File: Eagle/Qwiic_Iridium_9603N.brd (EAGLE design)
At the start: 50.8 x 50.8 mm, 72 parts, among them J1 SS4-10-3.50-X-D, J3 PTH, J6 ISP, J7 U.FL, Q1 DMG3415U-7, Q2 2N2222, U1 ATTINY84-ARDUINO, U2 LTC3225EDDB#TRMPBF

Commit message: Updates for V2 of the PCB
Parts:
- removed S1, S2: STANDOFF_ELECTRICALMCMASTER-95117A411, SparkFun-Electromechanical:STANDOFF-ELECTRICAL-MCMASTER-95117A411
- removed U$47: (no value), Labels:QWIIC-LOGO-MEDIUM
- added J8: (no value), SparkFun-Connectors:1X01_NO_SILK
- added U$10: (no value), 9603N_POWER:9603N_POWER0
- added U$11, U$28: (no value), 5.3V_OUT:5#3V0
- added U$12, U$17: (no value), Qwiic_007:QWIIC0
- added U$13: (no value), 150mA:150MA0
- added U$14: (no value), Charge:CHARGE0
- added U$15: (no value), Current:CURRENT0
- added U$18, U$19: (no value), Iridium_007:IRIDIUM0
- added U$2: (no value), POWER:POWER0
- added U$20, U$24: (no value), 9603N_007:9603N0
- added U$25: (no value), Qwiic_Bubble:QWIIC0
- added U$9: (no value), CHARGING:CHARGING0
- ANTENNA: device con-coax:J502-ND-142-0711-821/826 -> Qwiic_Iridium_9603N:J502-ND-142-0711-821/826
- J1: value SS4-10-3.50-X-D -> IRIDIUM_9603NIRIDIUM_9603N; device SS4-10-3.50-X-D:SS4-10-3.50-X-D -> Qwiic_Iridium_9603N:IRIDIUM_9603N
- U$1: device Labels:QWIIC-LOGO-MEDIUM -> 60mA:60MA0
- U$23: device buzzard_labels (3):QWIIC0 -> Qwiic_Bubble:QWIIC0
- U2: device LTC_By_element14_Batch_1:DFN300X200-10L -> Qwiic_Iridium_9603N:DFN300X200-10L
- moved J1 27.6 mm to (12.7, 8.89)
- moved U$1 11.8 mm to (44.7, 37.0), flipped to the top, turned to 90 degrees
- moved U$23 8.71 mm to (8.51, 21.2), turned to 90 degrees
- moved FRAME1 3.81 mm to (-7.62, -14.0)
- moved LOGO1 2.54 mm to (38.1, 2.54)
- moved J3 1.27 mm to (19.1, 1.27)
- moved J5 1.27 mm to (29.2, 1.27)
- moved U$16 1.27 mm to (29.2, 1.52)
- moved U$21 1.27 mm to (21.6, 1.65)
- moved U$22 1.27 mm to (19.1, 1.65)
- moved U$26 1.27 mm to (26.7, 1.65)
- moved U$27 1.27 mm to (24.1, 1.65)
- moved U$3 1.27 mm to (19.1, 1.65)
- moved U$4 1.27 mm to (21.6, 1.65)
- moved U$5 1.27 mm to (24.1, 1.65)
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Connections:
- net EXT_PWR: now also J8.1
- net GND: now also J1.HOLE1, J1.HOLE2; no longer S1.P1, S2.P1
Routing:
- net EXT_PWR: track 37.3 -> 58.4 mm
- net GND: track 35.8 -> 37.3 mm
- net 3.3V: track 131.4 -> 130.5 mm
- net SDA: track 93.1 -> 93.6 mm
- net !RST: track 51.7 -> 51.2 mm
- net SCL: track 88.2 -> 88.7 mm
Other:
- board text added: "V2"
- board text removed: "9603_Power"
- board text removed: "Charge Current 60mA 150mA"
- board text removed: "Charging"
- board text removed: "Power"
- board text removed: "Qwiic RockBLOCK 9603N"
- board text removed: "TPA2005D1"
- board text removed: "V1"

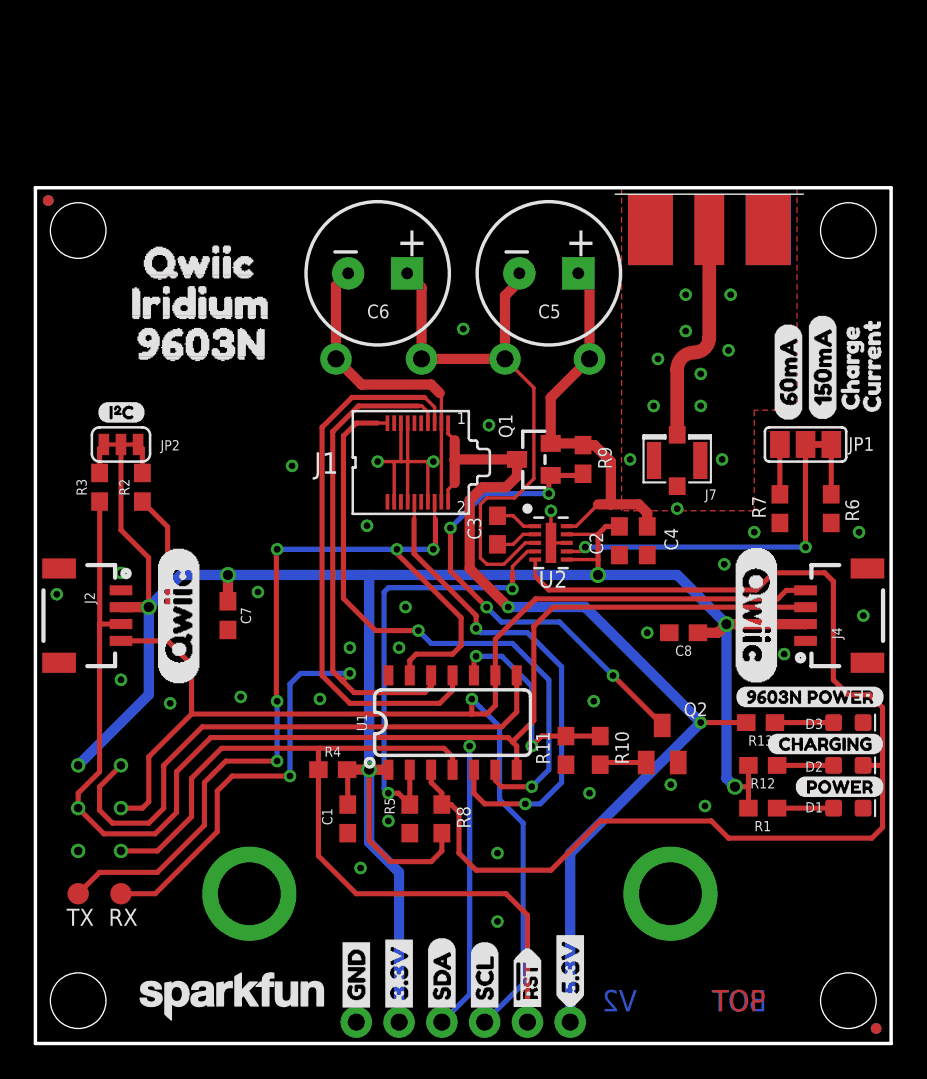
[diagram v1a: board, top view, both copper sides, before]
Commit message: Substantial update after testing the PCB
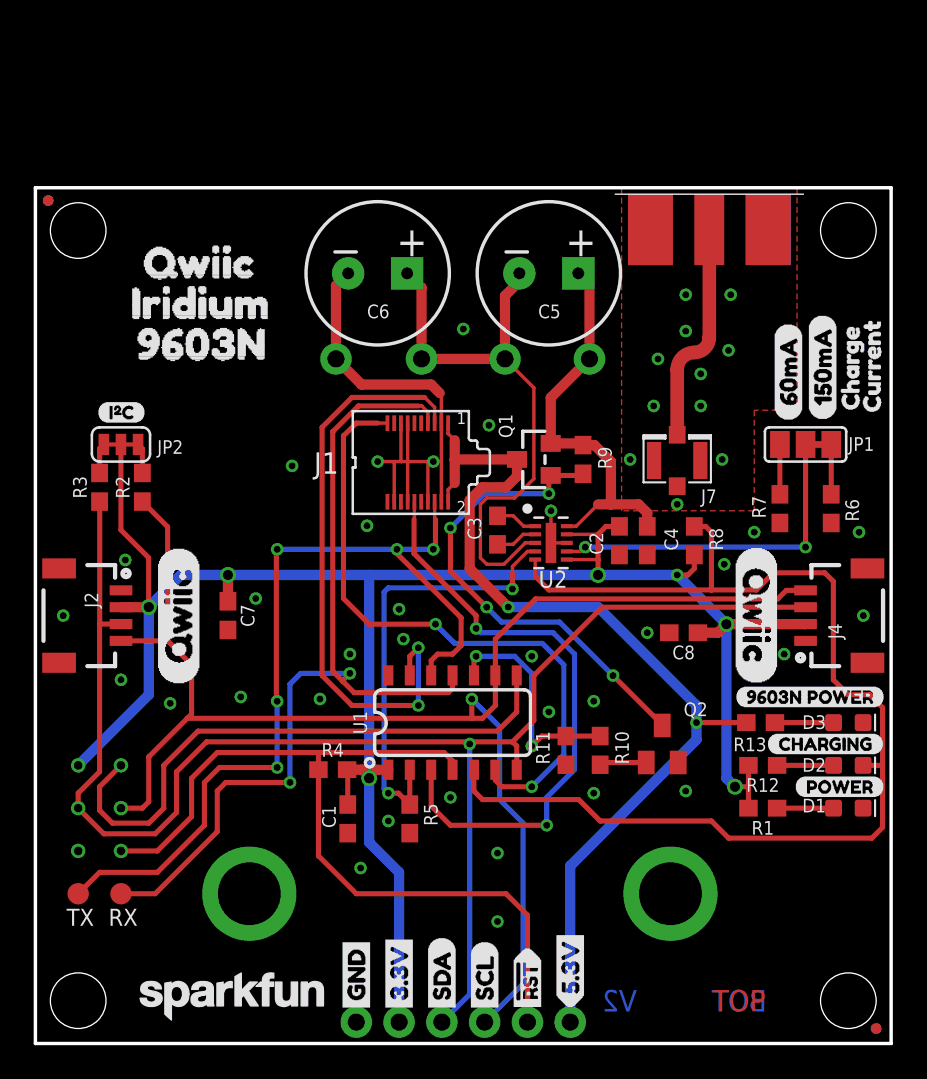
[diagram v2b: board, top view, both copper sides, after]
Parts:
- ANTENNA: value SMA-142-0711-821/826 -> SMA-; device Qwiic_Iridium_9603N:J502-ND-142-0711-821/826 -> Qwiic_Iridium_9603N:J502-ND-142-0711-821/826_NO_CREAM
- JP1: value (none) -> JUMPER-PAD-3-2OF3_NC_BY_TRACE_LARGE; device SparkFun-Passives:PAD-JUMPER-3-2OF3_NC_BY_TRACE_YES_SILK_LARGE -> Qwiic_Iridium_9603N:PAD-JUMPER-3-2OF3_NC_BY_TRACE_YES_SILK_LARGE
- U1: value ATTINY84-ARDUINO -> ATTINY841-ARDUINO; device SparkFun-IC-Microcontroller:SO14 -> Qwiic_Iridium_9603N:SO14
- moved R8 22.3 mm to (39.1, 29.8)
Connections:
- net ON_OFF: now also U1.13; no longer U1.11
- net PGOOD: now also U1.5; no longer U1.3
- net RI: now also U1.3; no longer U1.5
- net RX(OUT): now also U1.11; no longer U1.12
- net TX(IN): now also U1.12; no longer U1.13
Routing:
- net 3.3V: track 130.5 -> 122.7 mm, vias 6 -> 7
- net RI: track 29.3 -> 35.9 mm
- net SDA: track 93.6 -> 91.4 mm
- net ON_OFF: track 33.0 -> 35.1 mm, vias 0 -> 2
- net PGOOD: track 70.8 -> 68.9 mm
- net NA: track 36.5 -> 38.3 mm
- net RX(OUT): track 52.7 -> 54.3 mm
- net TX(IN): track 52.9 -> 51.9 mm
- net !RST: track 51.2 -> 50.5 mm
- net SCL: track 88.7 -> 89.3 mm
- net GND: vias 42 -> 44

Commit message: Added the ADM4210
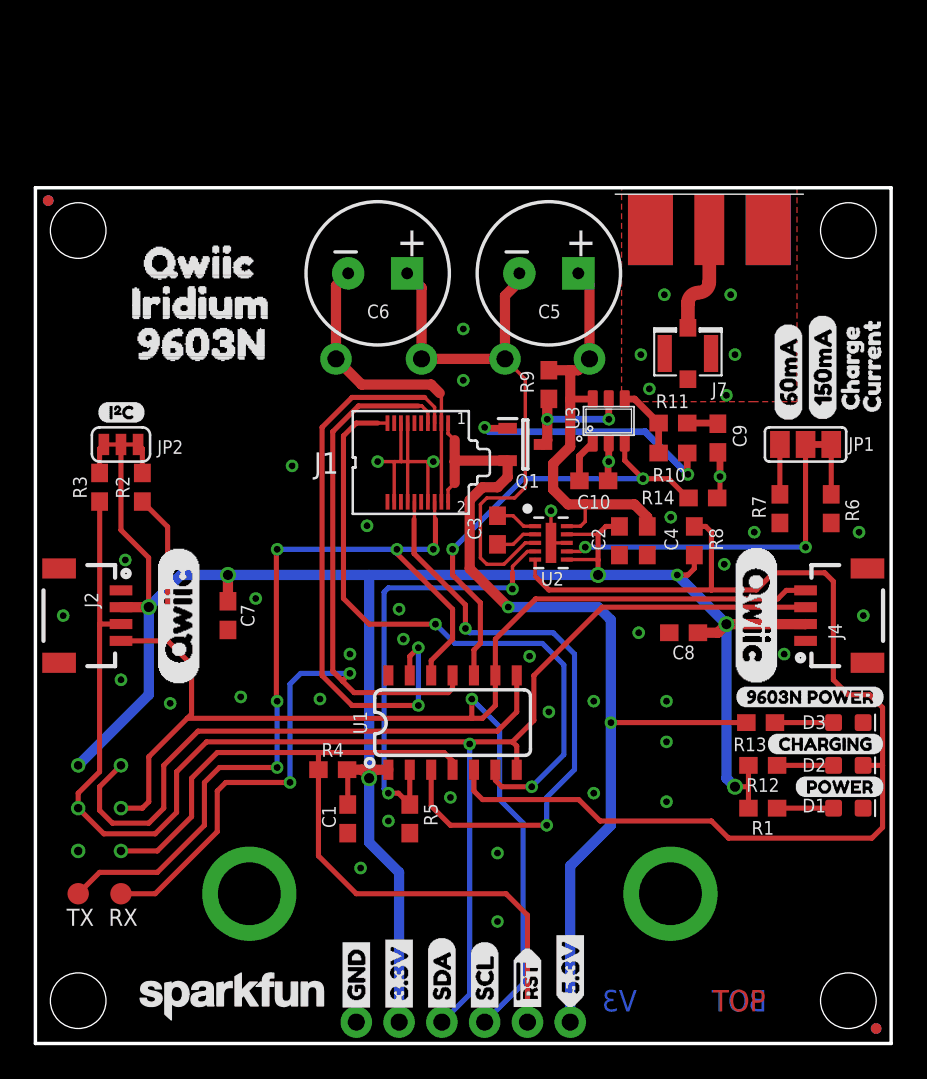
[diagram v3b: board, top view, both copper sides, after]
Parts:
- removed Q2: 2N2222, transistor:SOT23-BEC
- added C10: 0.22uF, SparkFun-Capacitors:0603
- added C9: 10nF, SparkFun-Capacitors:0603
- added R14: 10k, SparkFun-Resistors:0603
- added U3: ADM4210-1, ADM4210:TSOT6
- J1: value IRIDIUM_9603NIRIDIUM_9603N -> IRIDIUM_9603N
- Q1: value DMG3415U-7 -> DMG3414U-7; device microbuilder:SOT23-WIDE -> DMG3414U-7:SOT96P240X100-3N
- R10: value 1k -> 100
- R11: value 10k -> 100
- R9: value 10k -> 0.012 Ohm
- moved R11 20.4 mm to (37.8, 36.8), turned to 0 degrees
- moved R10 18.2 mm to (37.8, 35.1), turned to 180 degrees
- moved J7 6.38 mm to (38.7, 41.0)
- moved R9 4.89 mm to (30.5, 39.1), turned to 90 degrees
- moved Q1 1.02 mm to (29.1, 35.6), turned to 0 degrees
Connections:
- removed net N$19: Q1.1, Q2.C, R9.2
- removed net N$20: Q2.B, R10.2
- new net N$12: Q1.1, R10.1
- new net N$13: R10.2, R11.1, U3.4
- new net N$14: C9.1, R11.2
- new net N$15: C10.1, U3.1
- new net N$8: Q1.3, R9.1, U3.5
- net EXT_PWR: now also Q1.2; no longer Q1.3
- net GND: now also C10.2, C9.2, R14.2, U3.2; no longer Q2.E, R11.2
- net LTC3225_VOUT: now also R9.2, U3.6; no longer Q1.2, R9.1
- net PWR_EN: now also R14.1, U3.3; no longer R10.1, R11.1
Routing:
- net N$19: track 28.7 -> 0.00 mm, vias 4 -> 0
- net N$12: track 0.00 -> 15.9 mm, vias 0 -> 2
- net PWR_EN: track 13.5 -> 27.1 mm
- net N$8: track 0.00 -> 7.71 mm, vias 0 -> 2
- net N$7: track 13.0 -> 6.34 mm
- net GND: track 37.3 -> 42.4 mm
- net N$13: track 0.00 -> 4.38 mm
- net N$20: track 2.79 -> 0.00 mm
- net N$15: track 0.00 -> 2.58 mm
- net N$14: track 0.00 -> 1.83 mm
- net LTC3225_VOUT: track 24.2 -> 25.9 mm
- net TX(IN): track 51.9 -> 50.9 mm
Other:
- board text added: "V3"
- board text removed: "V2"

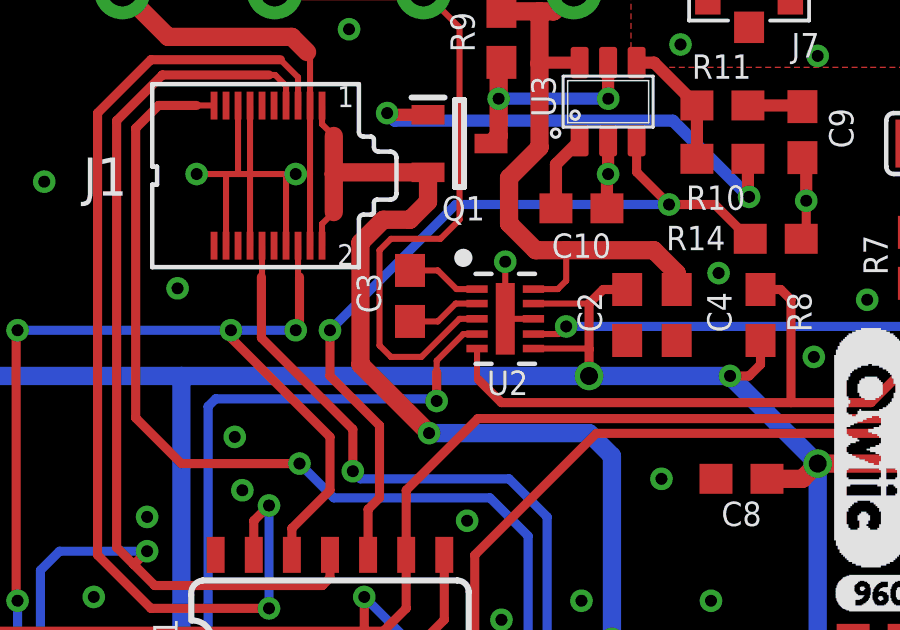
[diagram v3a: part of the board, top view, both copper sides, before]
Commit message: Added assembly details for V3 of the PCB
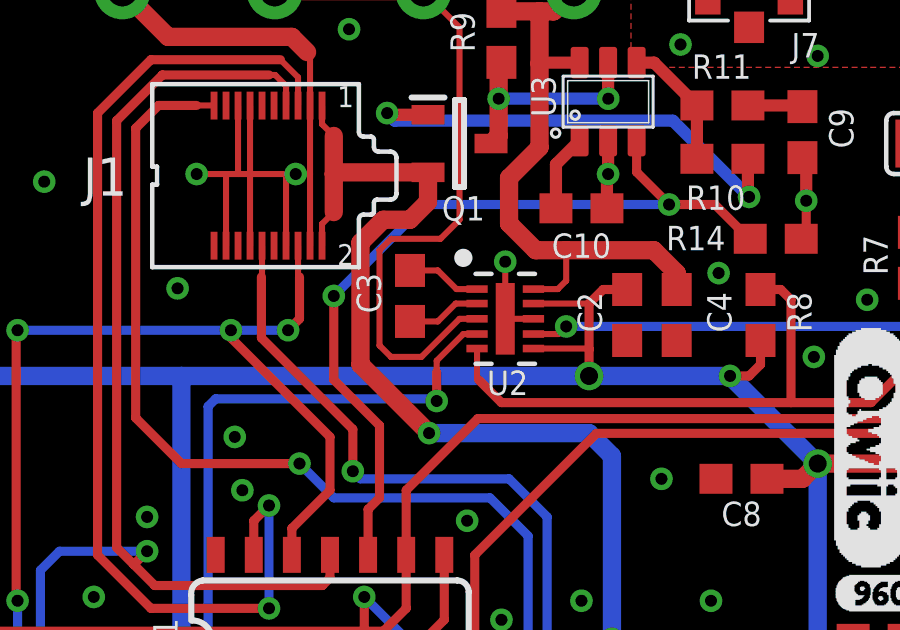
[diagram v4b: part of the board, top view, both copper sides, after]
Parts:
- C10: value 0.22uF -> 1.0uF
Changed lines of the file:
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@@
 <attribute name="PROD_ID" value="CAP-00867" x="40.513" y="35.941" size="1.778" layer="27" rot="R270" display="off"/>
 </element>
-<element name="C10" library="SparkFun-Capacitors" library_urn="urn:adsk.eagle:library:510" package="0603" package3d_urn="urn:adsk.eagle:package:37414/1" value="0.22uF" x="33.147" y="33.401" smashed="yes">
+<element name="C10" library="SparkFun-Capacitors" library_urn="urn:adsk.eagle:library:510" package="0603" package3d_urn="urn:adsk.eagle:package:37414/1" value="1.0uF" x="33.147" y="33.401" smashed="yes">
 <attribute name="NAME" x="33.147" y="31.75" size="0.8128" layer="25" font="vector" ratio="18" align="bottom-center"/>
-<attribute name="PROD_ID" value="CAP-07822" x="33.147" y="33.401" size="1.778" layer="27" display="off"/>
+<attribute name="PROD_ID" value="CAP-00868" x="33.147" y="33.401" size="1.778" layer="27" display="off"/>
 </element>
 <element name="R14" library="SparkFun-Resistors" library_urn="urn:adsk.eagle:library:532" package="0603" package3d_urn="urn:adsk.eagle:package:39650/1" value="10k" x="39.624" y="32.385" smashed="yes">
@@
 <wire x1="24.765" y1="24.003" x2="24.765" y2="25.781" width="0.3048" layer="1"/>
 <via x="21.463" y="29.337" extent="1-16" drill="0.4"/>
-<wire x1="21.463" y1="29.337" x2="23.622" y2="29.337" width="0.3048" layer="16"/>
-<via x="23.622" y="29.337" extent="1-16" drill="0.4"/>
-<wire x1="23.622" y1="29.337" x2="23.749" y2="29.464" width="0.3048" layer="1"/>
-<wire x1="23.749" y1="31.115" x2="23.749" y2="29.464" width="0.3048" layer="1"/>
+<wire x1="21.463" y1="29.337" x2="23.368" y2="29.337" width="0.3048" layer="16"/>
+<via x="23.368" y="29.337" extent="1-16" drill="0.4"/>
+<wire x1="23.368" y1="29.337" x2="23.749" y2="29.718" width="0.3048" layer="1"/>
+<wire x1="23.749" y1="31.115" x2="23.749" y2="29.718" width="0.3048" layer="1"/>
 <wire x1="24.765" y1="25.781" x2="21.463" y2="29.083" width="0.3048" layer="1"/>
 <wire x1="21.463" y1="29.083" x2="21.463" y2="29.337" width="0.3048" layer="1"/>
@@
 <wire x1="26.035" y1="23.368" x2="26.416" y2="23.749" width="0.3048" layer="1"/>
 <wire x1="26.416" y1="23.749" x2="26.416" y2="26.162" width="0.3048" layer="1"/>
-<wire x1="24.765" y1="27.813" x2="24.765" y2="29.337" width="0.3048" layer="1"/>
-<via x="24.765" y="29.337" extent="1-16" drill="0.4"/>
-<wire x1="24.765" y1="29.337" x2="28.956" y2="33.528" width="0.3048" layer="16"/>
+<wire x1="24.892" y1="27.686" x2="24.892" y2="30.48" width="0.3048" layer="1"/>
+<via x="24.892" y="30.48" extent="1-16" drill="0.4"/>
+<wire x1="24.892" y1="30.48" x2="27.94" y2="33.528" width="0.3048" layer="16"/>
 <via x="36.068" y="33.528" extent="1-16" drill="0.4"/>
 <wire x1="36.068" y1="33.528" x2="34.986" y2="34.61" width="0.3048" layer="1"/>
 <wire x1="34.986" y1="34.61" x2="34.986" y2="35.657" width="0.3048" layer="1"/>
-<wire x1="26.416" y1="26.162" x2="24.765" y2="27.813" width="0.3048" layer="1"/>
-<wire x1="28.956" y1="33.528" x2="36.068" y2="33.528" width="0.3048" layer="16"/>
+<wire x1="26.416" y1="26.162" x2="24.892" y2="27.686" width="0.3048" layer="1"/>
+<wire x1="27.94" y1="33.528" x2="36.068" y2="33.528" width="0.3048" layer="16"/>
 <contactref element="R14" pad="1"/>
 <wire x1="38.774" y1="32.385" x2="38.735" y2="32.385" width="0.3048" layer="1"/>
